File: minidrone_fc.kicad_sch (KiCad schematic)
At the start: 36 parts, among them J1 BATT, J2 MOTOR_FL, J3 MOTOR_FR, J4 MOTOR_RL, J5 MOTOR_RR, Q1 AO3400A, Q2 AO3400A, Q3 AO3400A, Q4 AO3400A, U1 XIAO_ESP32C3, U2 GY-521, U3 BMP280

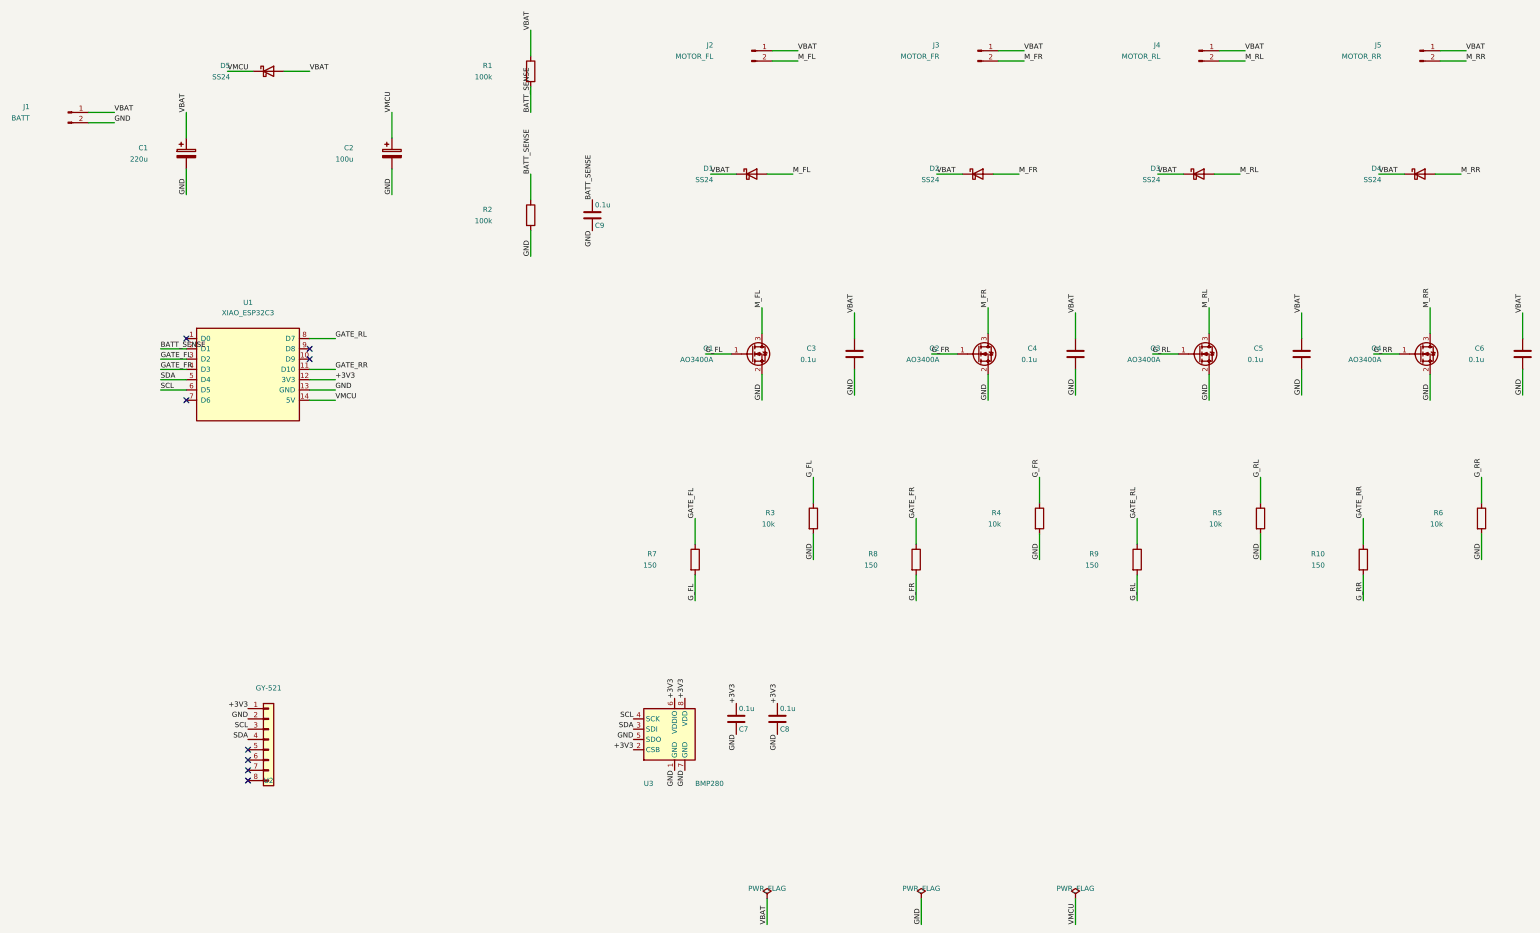
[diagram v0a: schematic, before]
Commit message: rev2.1: 昇降圧DC-DC(TPS63002)を追加し4層化
## なぜ

改訂前の基板には昇圧素子が1つもなく、電池電圧が「3.3V + LDOドロップアウト」
を下回れば 3V3 レールは必ず追従して下がる構造だった。
8520コアレスモーター4個で 6.5A を引くと電池は 3.7V→3.4V に沈み、
そこから D5(SS24) の 0.4V を引いて VMCU ≈ 3.0V、
さらに XIAO 内蔵 LDO のドロップアウトを引くと 3V3 は 2.8〜2.95V。
ESP32-C3 の動作下限 3.0V を公称電圧ですら下回っており、
スロットルを上げた瞬間に MCU がリセットする状態だった。

## 何を変えたか

- U4 TPS63002 (昇降圧・5V固定) を VBAT と XIAO の "5V" ピンの間に挿入
  L1 2.2uH / C10 10uF(in) / C11 22uF(out) / C12 0.1uF(VINA)
  電池 3.0V でも出力5V。D5 で 0.4V 落ちても 4.6V が XIAO に入り、
  内蔵LDO が 3.3V を作るのに必要な 3.5V に対し余裕1V以上
- D5 は流用。向きも不変で、上流が VBAT から V5V に変わっただけ
- 4層化: In1.Cu = ベタGND 全面 2949mm2 / In2.Cu = VBAT プレーン 全面 2811mm2
  6.5A を 0.6mm トレースで流していた状態を解消
- GND スティッチングビア 133本を衝突判定付きで自動配置
- U4 にローカルクリアランス 0.1mm を設定
  VSON-10 は 0.5mmピッチでパッド間 0.22mm しかなく、VBAT が属する
  Power ネットクラスの 0.25mm 要求を物理的に満たせないため。
  Power の 0.25mm はモーター大電流の配線・ベタ向けポリシーであり、
  ファインピッチICのピン間に適用する意図ではない (JLCPCB 製造限界 0.1mm)

+3V3 / VMCU / GATE_* / M_* / SCL / SDA は一切変更していない。
既存部品のパッド-ネット変更は D5 pad2 の VBAT→V5V ただ1箇所。

## 検証 (kicad-cli)

                    改訂前          改訂後
  DRC 違反          32 (warning)    37 (warning) ※増分5はすべてシルク重なり
  DRC エラー        0               0
  未配線            4               1  (改善)
  schematic_parity  0               0  (回路図と基板が完全一致)
  ERC               warning 5/err 0 warning 5/err 0 (同一)

## 残課題

- 未配線1件 (GNDベタの孤立島)。電気的な害はない
- シルク警告5件。C10/C11/C12 のリファレンス文字が隣接銅箔に重なる。
  この一角は部品とビアで埋まっており逃がす余地がない
- Gerber / BOM / 実装座標は未再出力。4層として出し直しが必要
- 実機でのブラウンアウト解消は未検証

詳細は README.md 第9節と docs/superpowers/plans/2026-09-19-buckboost-and-4layer.md

Co-Authored-By: Claude Opus 5 <noreply@anthropic.com>
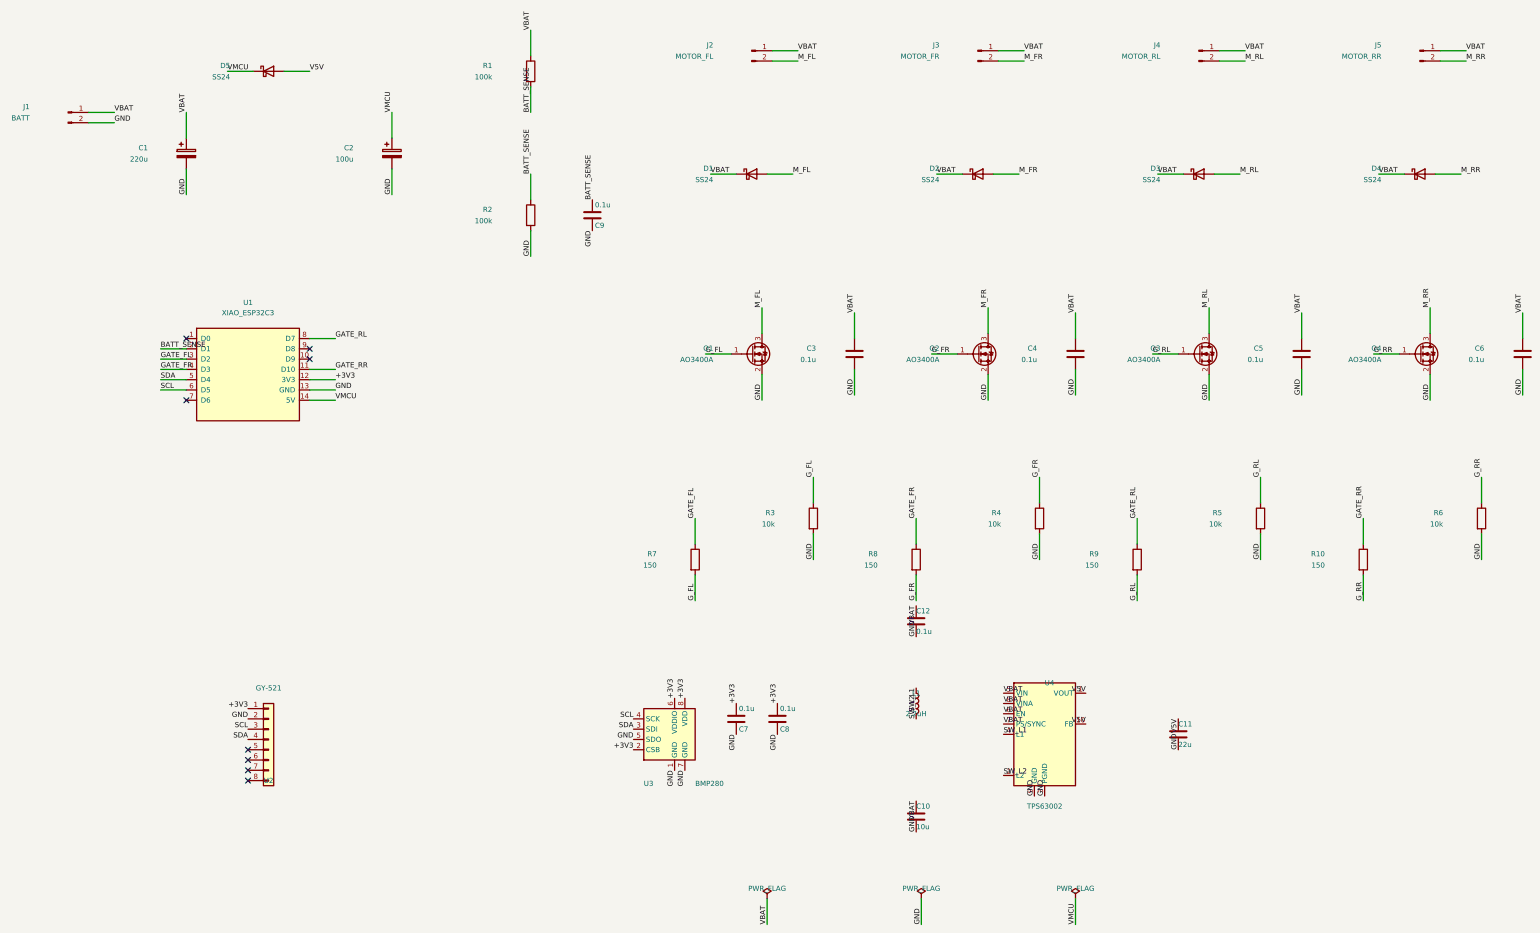
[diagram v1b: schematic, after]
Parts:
- added C10: 10u, Capacitor_SMD:C_0805_2012Metric, symbol Device:C
- added C11: 22u, Capacitor_SMD:C_0805_2012Metric, symbol Device:C
- added C12: 0.1u, Capacitor_SMD:C_0603_1608Metric, symbol Device:C
- added L1: 2.2uH, Inductor_SMD:L_APV_ANR3015, symbol Device:L
- added U4: TPS63002, Package_SON:VSON-10-1EP_3x3mm_P0.5mm_EP1.65x2.4mm_ThermalVias, symbol Regulator_Switching:TPS63002
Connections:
- net GND: now also C10.2, C11.2, C12.2, U4.11 (PGND), U4.3 (PGND), U4.9 (GND)
- net VBAT: now also C10.1, C12.1, U4.5 (VIN), U4.6 (EN), U4.7 (PS/SYNC), U4.8 (VINA); no longer D5.2 (A)
- new net SW_L1: L1.1, U4.4 (L1)
- new net SW_L2: L1.2, U4.2 (L2)
- new net V5V: C11.1, D5.2 (A), U4.1 (VOUT), U4.10 (FB)

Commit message: bom: 新規部品4点に LCSC 品番を追加
4層での製造データ再出力にあたり、rev2.1 で追加した部品に
JLCPCB の品番が未設定で BOM が不完全だったため設定。

  U4  TPS63002DRCR      C116655   VSON-10-EP(3x3) 在庫1153
  L1  NRS3015T2R2MNGHV  C1329483  2.2uH/1.5A/3x3mm AEC-Q200 在庫506
  C10 10uF 25V X5R 0805 C15850    Basic part (実装無料) 在庫350万
  C11 22uF 16V X5R 0805 C128856   在庫20058
  C12 0.1uF 0603        C14663    C3-C9 と同一品

プロパティ追加のみで結線は不変。
ネットリスト 22ネット / V5V 4ピン / +3V3 7ピン で変更前と一致、
ERC も warning 5 / error 0 で同一であることを確認済み。

Co-Authored-By: Claude Opus 5 <noreply@anthropic.com>
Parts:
- C10: LCSC (none) -> C15850
- C11: LCSC (none) -> C128856
- C12: LCSC (none) -> C14663; MPN (none) -> CC0603KRX7R9BB104
- L1: LCSC (none) -> C1329483; MPN (none) -> NRS3015T2R2MNGHV
- U4: LCSC (none) -> C116655; MPN (none) -> TPS63002DRCR
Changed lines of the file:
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@@
 			)
 		)
+    (property "LCSC" "C116655" (at 271.78 213.36 0)
+      (effects (font (size 1.27 1.27)) (hide yes))
+    )
+    (property "MPN" "TPS63002DRCR" (at 271.78 213.36 0)
+      (effects (font (size 1.27 1.27)) (hide yes))
+    )
 		(pin "1"
 		)
@@
 			)
 		)
+    (property "LCSC" "C1329483" (at 240.03 205.74 0)
+      (effects (font (size 1.27 1.27)) (hide yes))
+    )
+    (property "MPN" "NRS3015T2R2MNGHV" (at 240.03 205.74 0)
+      (effects (font (size 1.27 1.27)) (hide yes))
+    )
 		(pin "1"
 		)
@@
 			)
 		)
+    (property "LCSC" "C15850" (at 240.03 233.68 0)
+      (effects (font (size 1.27 1.27)) (hide yes))
+    )
 		(pin "1"
 		)
@@
 			)
 		)
+    (property "LCSC" "C128856" (at 304.8 213.36 0)
+      (effects (font (size 1.27 1.27)) (hide yes))
+    )
 		(pin "1"
 		)
@@
 			)
 		)
-		(pin "1"
-		)
+    (property "LCSC" "C14663" (at 240.03 185.42 0)
+      (effects (font (size 1.27 1.27)) (hide yes))
+    )
+    (property "MPN" "CC0603KRX7R9BB104" (at 240.03 185.42 0)
+      (effects (font (size 1.27 1.27)) (hide yes))
+    )
+		(pin "1"
+		)

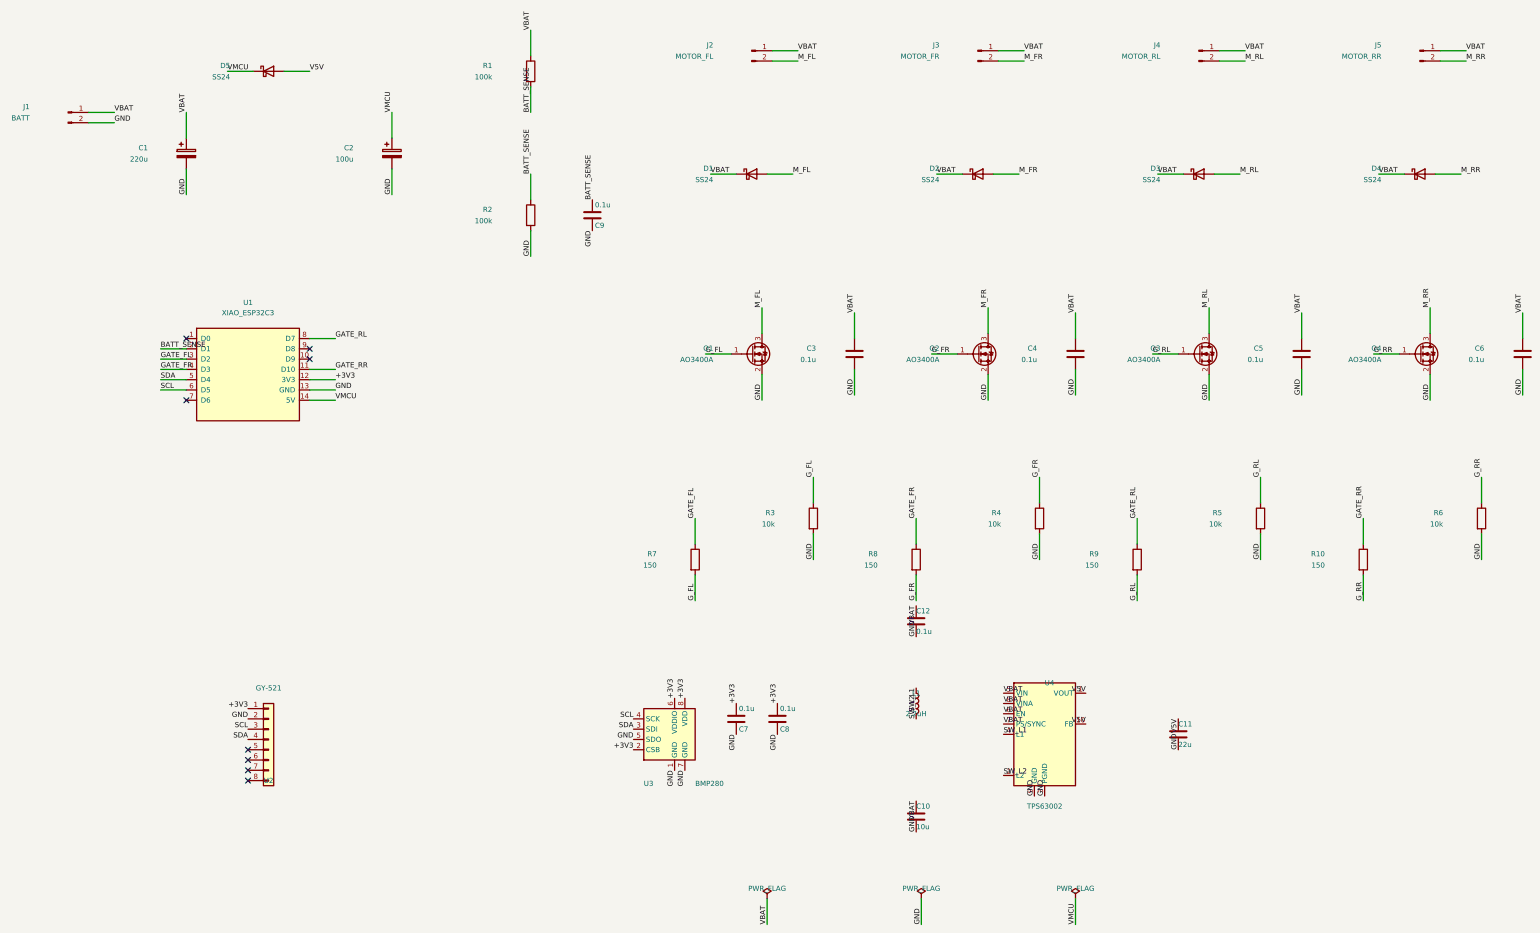
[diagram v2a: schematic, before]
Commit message: rev3: 回路図を全面刷新し、29x29mm 4層基板の骨格を作成
rev2.1 (50x64mm / 取付穴44x44mm) を Tiny Whoop 標準ピッチに作り直す。
回路図は rev2 の内容を破棄して一から構成した（rev2.1 は main に保全）。

## 回路図（ERC エラー0 / 32ネット / 55部品）

  XIAO ESP32C3 (DIP) -> ESP32-C3-MINI-1 (SMD, 基板内蔵アンテナ)
  GY-521 モジュール   -> BMI270 直付け (SPI)
  BMP280              -> SPI に変更し IMU とバス共用
  TPS63002(5V)+LDO    -> TPS63001 で 3.3V 一段
  電解コンデンサ      -> 積層セラミック
  USB-C (TYPE-C-31-M-12) + USBLC6 を新規搭載

安全上の要点: 充電回路を載せないため、電池側に逆流防止ダイオード D5 を
入れて USB の 5V が LiPo に流れ込むのを防ぐ。VBAT(19ピン) と VSYS(13ピン)
が別ネットであることを確認済み（統合されると D5 が短絡し過充電になる）。

## 基板

  29 x 29 mm / 角R3 / 板厚 0.8mm / 4層
  取付穴 φ1.5mm x4 を 25.5 x 25.5mm ピッチ（Whoop 標準）
  schematic_parity: 0

## 作業中に修正した不具合

1. create_board_from_schematic が no-connect ピンに隣接ネットを割り当てた
   U1/4 -> GATE_FR, U1/7 -> GATE_RL, U2/9 -> GND, U2/11 -> GND
   rev2 でも U1/7 に GATE_RL という同一症状。再現性のある MCP の不具合。
   通常の DRC では検出できず schematic_parity でのみ分かる。
   U2/11 (OSDO) は BMI270 の出力ピンで、GND 固定のままだと危険だった。

2. D1-D4 を SS24(SMA) から DSS24(SOD-123FL) に変更
   SMA はコートヤード 7.09x3.59mm で、幅7mmの四隅に FET と同居できなかった。
   仕様書7節で想定していた置き換え。定格 2A/40V は同等、4個で 58mm² 削減。
   LCSC: C115726 -> C2923950 (在庫125,283)

3. 仕様書・計画書の J1 シンボル名の誤りを訂正
   フットプリント名を書いていた。正しくは Connector:Conn_01x02_Pin。

## 未完了

Task 9（配置）で同一面の干渉が51件残っている。
Task 10（配線）、11（DRC）、12（製造データ）は未着手。

Co-Authored-By: Claude Opus 5 <noreply@anthropic.com>
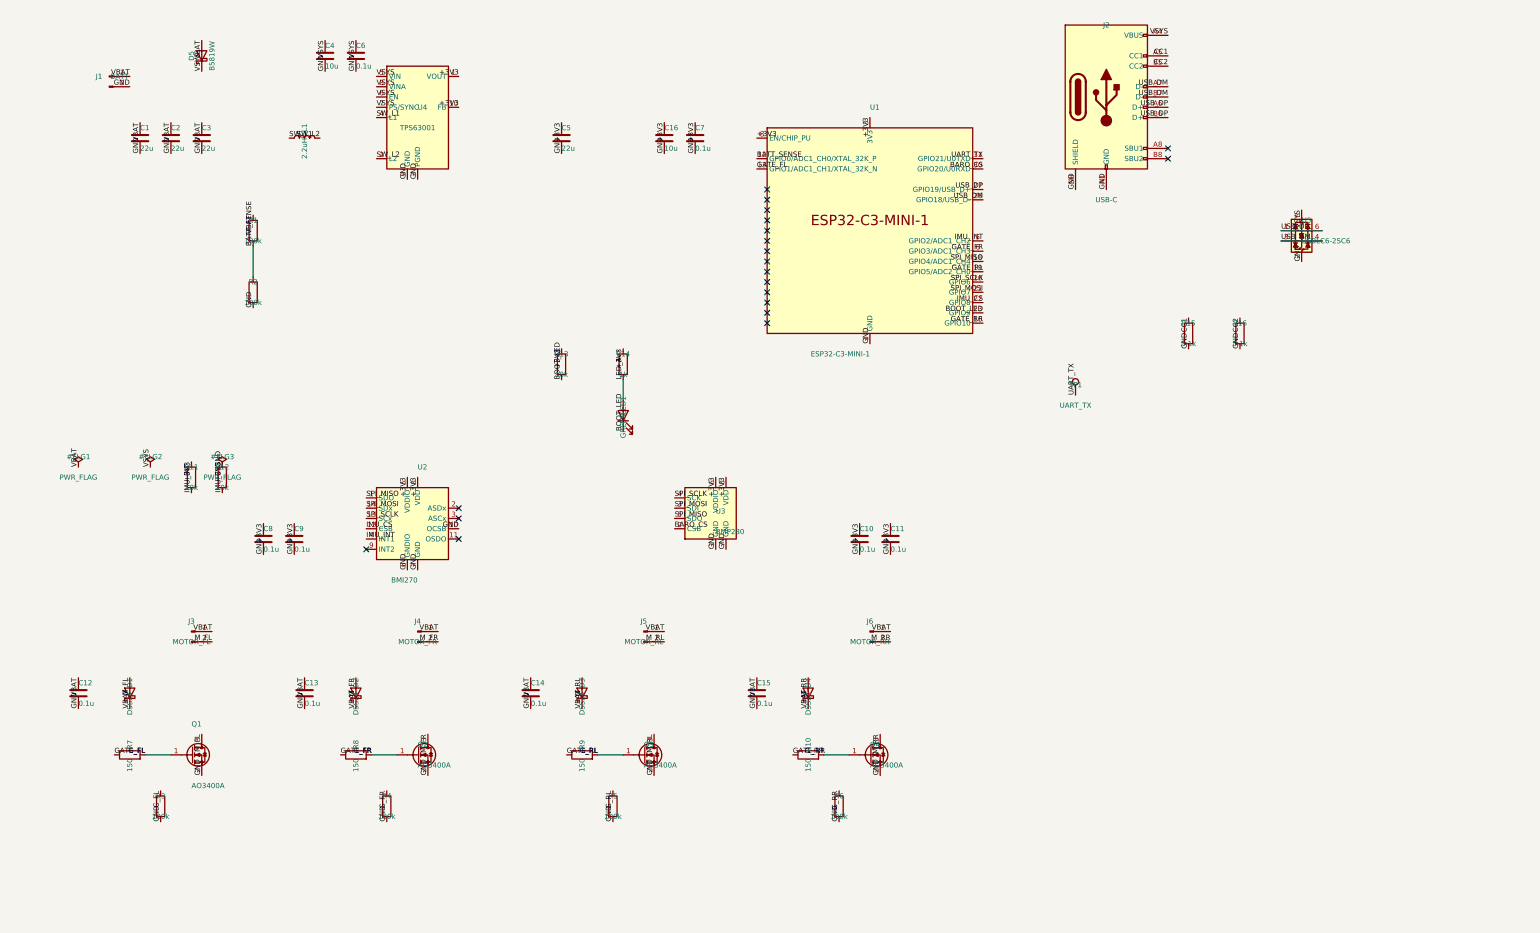
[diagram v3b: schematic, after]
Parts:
- removed C1: 220u, Capacitor_SMD:CP_Elec_6.3x5.3, symbol Device:C_Polarized
- removed C2: 100u, Capacitor_SMD:CP_Elec_6.3x5.3, symbol Device:C_Polarized
- removed D5: SS24, Diode_SMD:D_SMA, symbol Diode:SS24
- removed J2: MOTOR_FL, TestPoint:TestPoint_2Pads_Pitch2.54mm_Drill0.8mm, symbol Connector:Conn_01x02_Pin
- removed U1: XIAO_ESP32C3, seeed:XIAO-ESP32-C3-DIP, symbol minidrone:XIAO_ESP32C3
- removed U2: GY-521, Connector_PinHeader_2.54mm:PinHeader_1x08_P2.54mm_Vertical, symbol Connector_Generic:Conn_01x08
- removed U4: TPS63002, Package_SON:VSON-10-1EP_3x3mm_P0.5mm_EP1.65x2.4mm_ThermalVias, symbol Regulator_Switching:TPS63002
- added C1, C2: 22u, Capacitor_SMD:C_0805_2012Metric, symbol Device:C
- added C13, C14, C15: 0.1u, Capacitor_SMD:C_0603_1608Metric, symbol Device:C
- added C16: 10u, Capacitor_SMD:C_0805_2012Metric, symbol Device:C
- added D5: B5819W, Diode_SMD:D_SOD-123, symbol Device:D_Schottky
- added J2: USB-C, Connector_USB:USB_C_Receptacle_HRO_TYPE-C-31-M-12, symbol Connector:USB_C_Receptacle_USB2.0_16P
- added J6: MOTOR_RR, TestPoint:TestPoint_2Pads_Pitch2.54mm_Drill0.8mm, symbol Connector:Conn_01x02_Pin
- added LED1: GREEN, LED_SMD:LED_0603_1608Metric, symbol Device:LED
- added R11, R12, R13: 10k, Resistor_SMD:R_0603_1608Metric, symbol Device:R
- added R14: 1k, Resistor_SMD:R_0603_1608Metric, symbol Device:R
- added R15, R16: 5.1k, Resistor_SMD:R_0603_1608Metric, symbol Device:R
- added TP1: UART_TX, TestPoint:TestPoint_Pad_D1.0mm, symbol Connector:TestPoint
- added U1: ESP32-C3-MINI-1, Espressif:ESP32-C3-MINI-1, symbol Espressif:ESP32-C3-MINI-1
- added U2: BMI270, Package_LGA:Bosch_LGA-14_3x2.5mm_P0.5mm, symbol Sensor_Motion:BMI160
- added U4: TPS63001, Package_SON:VSON-10-1EP_3x3mm_P0.5mm_EP1.65x2.4mm_ThermalVias, symbol Regulator_Switching:TPS63001
- added U5: USBLC6-2SC6, Package_TO_SOT_SMD:SOT-23-6, symbol Power_Protection:USBLC6-2SC6
- C10: value 10u -> 0.1u; footprint Capacitor_SMD:C_0805_2012Metric -> Capacitor_SMD:C_0603_1608Metric; LCSC C15850 -> C14663
- C11: value 22u -> 0.1u; footprint Capacitor_SMD:C_0805_2012Metric -> Capacitor_SMD:C_0603_1608Metric; LCSC C128856 -> C14663
- C12, C6, C7, C8, C9: MPN CC0603KRX7R9BB104 -> (none)
- C3, C5: value 0.1u -> 22u; footprint Capacitor_SMD:C_0603_1608Metric -> Capacitor_SMD:C_0805_2012Metric; LCSC C14663 -> C128856; MPN CC0603KRX7R9BB104 -> (none)
- C4: value 0.1u -> 10u; footprint Capacitor_SMD:C_0603_1608Metric -> Capacitor_SMD:C_0805_2012Metric; LCSC C14663 -> C15850; MPN CC0603KRX7R9BB104 -> (none)
- D1, D2, D3, D4: value SS24 -> DSS24; footprint Diode_SMD:D_SMA -> Diode_SMD:D_SOD-123F; LCSC C115726 -> C2923950; MPN SS24 -> DSS24
- J1: Manufacturer JST -> (none)
- J3: value MOTOR_FR -> MOTOR_FL; Notes Motor wire solder pads - no component -> (none); dnp 1 -> (none)
- J4: value MOTOR_RL -> MOTOR_FR; Notes Motor wire solder pads - no component -> (none); dnp 1 -> (none)
- J5: value MOTOR_RR -> MOTOR_RL; Notes Motor wire solder pads - no component -> (none); dnp 1 -> (none)
- Q1, Q2, Q3, Q4: Manufacturer Alpha & Omega -> (none)
- R1, R2: MPN 0603WAF1003T5E -> (none)
- R10, R7, R8, R9: MPN 0603WAF1500T5E -> (none)
- R3, R4, R5, R6: value 10k -> 100k; LCSC C130232 -> C25803; MPN RK73H1JTTD1002F -> (none)
- U3: MPN WF282A -> BMP280; Notes BMP280-compatible barometer, I2C addr 0x76 (SDO=GND, CSB=3V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 -> (none)
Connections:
- net V5V is gone; now on net +3V3: C11.1
- net +3V3: now also C10.1, C5.1, C9.1, C16.1, R11.1, R12.1, R13.1, R14.1, U1.3 (3V3), U1.8 (EN/CHIP_PU), U2.5 (VDDIO), U2.8 (VDD), U4.1 (VOUT), U4.10 (FB); no longer U3.2 (CSB)
- net BATT_SENSE: now also U1.12 (GPIO0/ADC1_CH0/XTAL_32K_P); no longer C9.1
- net GATE_FL: now also U1.13 (GPIO1/ADC1_CH1/XTAL_32K_N)
- net GATE_FR: now also U1.6 (GPIO3/ADC1_CH3)
- net GATE_RL: now also U1.19 (GPIO5/ADC2_CH0)
- net GATE_RR: now also U1.16 (GPIO10)
- net GND: now also C1.2, C13.2, C14.2, C15.2, C16.2, C2.2, J2.A1 (GND), J2.A12 (GND), J2.B1 (GND), J2.B12 (GND), J2.SH (SHIELD), R15.2, R16.2, U1.1 (GND), U1.11 (GND), U1.14 (GND), U1.2 (GND), U1.36 (GND), U1.37 (GND), U1.38 (GND), U1.39 (GND), U1.40 (GND), U1.41 (GND), U1.42 (GND), U1.43 (GND), U1.44 (GND), U1.45 (GND), U1.46 (GND), U1.47 (GND), U1.48 (GND), U1.49 (GND), U1.50 (GND), U1.51 (GND), U1.52 (GND), U1.53 (GND), U2.10 (OCSB), U2.6 (GNDIO), U2.7 (GND), U4.11 (PGND), U4.3 (PGND), U4.9 (GND), U5.2 (GND); no longer U3.5 (SDO)
- net M_FL: now also J3.2 (Pin_2)
- net M_FR: now also J4.2 (Pin_2); no longer J3.2 (Pin_2)
- net M_RL: now also J5.2 (Pin_2); no longer J4.2 (Pin_2)
- net M_RR: now also J6.2 (Pin_2); no longer J5.2 (Pin_2)
- net SW_L1: now also U4.4 (L1)
- net SW_L2: now also U4.2 (L2)
- net VBAT: now also C1.1, C13.1, C14.1, C15.1, C2.1, D5.2 (A), J6.1 (Pin_1); no longer C10.1, C4.1, C5.1, C6.1
- net SCL renamed SPI_SCLK
- net SPI_SCLK: now also U1.20 (GPIO6), U2.13 (SCx)
- net SDA renamed SPI_MOSI
- net SPI_MOSI: now also U1.21 (GPIO7), U2.14 (SDx)
- new net BARO_CS: U1.30 (GPIO20/U0RXD), U3.2 (CSB)
- new net BOOT_LED: LED1.1 (K), R13.2, U1.23 (GPIO9)
- new net CC1: J2.A5 (CC1), R15.1
- new net CC2: J2.B5 (CC2), R16.1
- new net IMU_CS: R12.2, U1.22 (GPIO8), U2.12 (CSB)
- new net IMU_INT: R11.2, U1.5 (GPIO2/ADC1_CH2), U2.4 (INT1)
- new net LED_A: LED1.2 (A), R14.2
- new net SPI_MISO: U1.18 (GPIO4/ADC1_CH4), U2.1 (SDO), U3.5 (SDO)
- new net UART_TX: TP1.1, U1.31 (GPIO21/U0TXD)
- new net USB_DM: J2.A7 (D-), J2.B7 (D-), U1.26 (GPIO18/USB_D-), U5.3 (I/O2), U5.4 (I/O2)
- new net USB_DP: J2.A6 (D+), J2.B6 (D+), U1.27 (GPIO19/USB_D+), U5.1 (I/O1), U5.6 (I/O1)
- new net VSYS: C4.1, C6.1, D5.1 (K), J2.A4 (VBUS), J2.A9 (VBUS), J2.B4 (VBUS), J2.B9 (VBUS), U4.5 (VIN), U4.6 (EN), U4.7 (PS/SYNC), U4.8 (VINA), U5.5 (VBUS)
- no-connect marks 8 -> 20
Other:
- title: Mini Drone Flight Controller -> (none)
